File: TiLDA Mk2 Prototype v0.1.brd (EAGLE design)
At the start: 67.9 x 100 mm, 199 parts, among them IC1 ATSAM3X8EA-AU, IC10 MCP73831, IC2 MPU-6050, IC3 SRF-V1.2, IC5 S25FL216K0PMFI011, IC7 HMC5883LSMD (NP), IC8 MCP1825T-3302E/DC, IC9 TC1015-3V3, J1 ZX62-AB-5PA(11), J3 Arduino Headers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

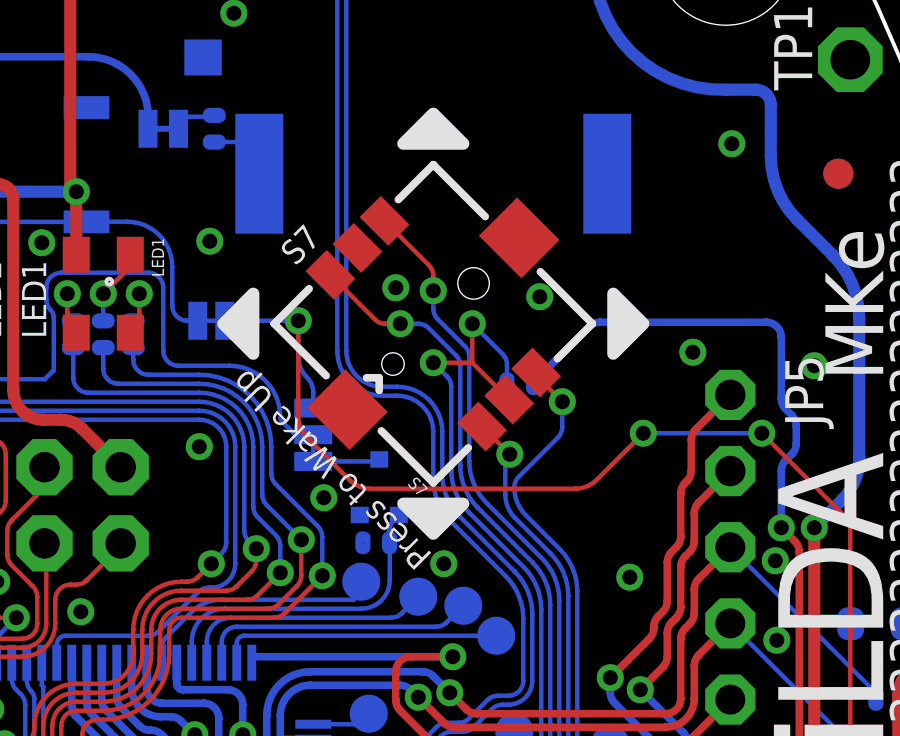
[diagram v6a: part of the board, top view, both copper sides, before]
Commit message: Parts: Joystick footprint Prototype: Joystick footprint
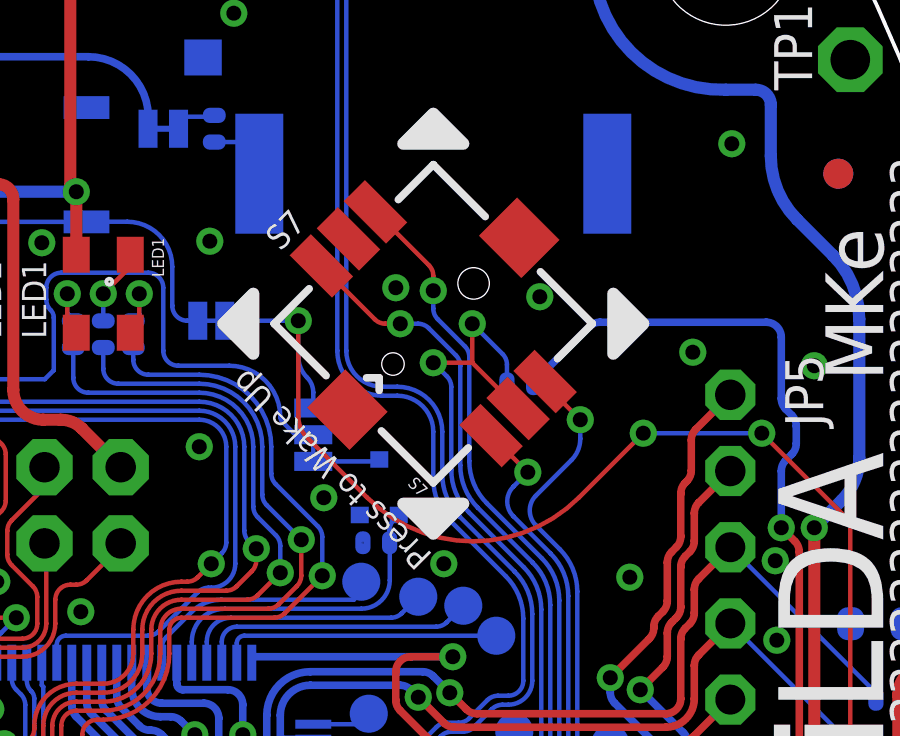
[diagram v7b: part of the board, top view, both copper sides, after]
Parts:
- S7: device TiLDA Mk2 Parts:JOYSTICK_MINI_ALPS -> TiLDA Mk2 Parts:JOYSTICK_MULTICOMP
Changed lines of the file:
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@@
 <text x="17.6" y="82.3" size="0.8128" layer="21" font="vector" ratio="15" rot="R90">S5</text>
 <text x="11.3" y="74.6" size="0.8128" layer="21" font="vector" ratio="15" rot="R90">S6</text>
-<text x="43.4" y="85.9" size="0.8128" layer="21" font="vector" ratio="15" rot="R45">S7</text>
+<text x="42.9" y="86.4" size="0.8128" layer="21" font="vector" ratio="15" rot="R45">S7</text>
 <text x="44.5" y="72.3" size="0.8128" layer="22" font="vector" ratio="15" rot="MR0">IC1</text>
 <text x="41.3" y="13.7" size="0.8128" layer="22" font="vector" ratio="15" rot="MR90">IC2</text>
@@
 <element name="S5" library="TiLDA Mk2 Parts" package="TACTILE_SWITCH_SMD" value="SKQGAKE010" x="20.5" y="83.9" rot="R90"/>
 <element name="S6" library="TiLDA Mk2 Parts" package="TACTILE_SWITCH_SMD" value="SKQGAKE010" x="14" y="77.9" rot="R90"/>
-<element name="S7" library="TiLDA Mk2 Parts" package="JOYSTICK_MINI_ALPS" value="SKRHAAE010" x="48" y="84" rot="R135"/>
+<element name="S7" library="TiLDA Mk2 Parts" package="JOYSTICK_MULTICOMP" value="SKRHAAE010" x="48" y="84" rot="R135"/>
 <element name="SJ5" library="TiLDA Mk2 Parts" package="SJ_3" value="RESET SELECT" x="37.4" y="38.8" rot="MR0"/>
 <element name="R21" library="TiLDA Mk2 Parts" package="R0402-ARDUINO-ROUND" value="0402/100K/1%" x="60.7" y="61.44" rot="MR0"/>
@@
 <wire x1="55" y1="80.35" x2="58.95" y2="80.35" width="0.15" layer="16"/>
 <wire x1="58.95" y1="80.35" x2="61.753553125" y2="77.546446875" width="0.15" layer="1"/>
-<wire x1="55" y1="80.35" x2="53.44289375" y2="78.79289375" width="0.15" layer="1"/>
-<wire x1="53.44289375" y1="78.79289375" x2="52.7357875" y2="78.5" width="0.15" layer="1" curve="-45"/>
-<wire x1="52.7357875" y1="78.5" x2="45.9142125" y2="78.5" width="0.15" layer="1"/>
-<wire x1="45.9142125" y1="78.5" x2="45.20710625" y2="78.79289375" width="0.15" layer="1" curve="-45"/>
-<wire x1="45.20710625" y1="78.79289375" x2="43.79289375" y2="80.20710625" width="0.15" layer="1"/>
+<wire x1="55" y1="80.35" x2="52.860534375" y2="78.210534375" width="0.15" layer="1"/>
+<wire x1="52.860534375" y1="78.210534375" x2="45.789465625" y2="78.210534375" width="0.15" layer="1" curve="-90"/>
+<wire x1="45.789465625" y1="78.210534375" x2="43.79289375" y2="80.20710625" width="0.15" layer="1"/>
 <wire x1="43.79289375" y1="80.20710625" x2="43.5" y2="80.9142125" width="0.15" layer="1" curve="-45"/>
 <wire x1="43.5" y1="80.9142125" x2="43.5" y2="84.1" width="0.15" layer="1"/>
@@
 <wire x1="48" y1="82.7" x2="48.453553125" y2="82.246446875" width="0.15" layer="16"/>
 <wire x1="48.453553125" y1="82.246446875" x2="48.6" y2="81.89289375" width="0.15" layer="16" curve="-45"/>
-<wire x1="50.52790625" y1="81.472090625" x2="49.3" y2="82.699996875" width="0.15" layer="1"/>
+<wire x1="50.828425" y1="81.171571875" x2="49.3" y2="82.699996875" width="0.15" layer="1"/>
 <wire x1="49.3" y1="82.699996875" x2="49.299996875" y2="82.7" width="0.15" layer="1"/>
 <wire x1="49.299996875" y1="82.7" x2="48" y2="82.7" width="0.15" layer="1"/>
@@
 <wire x1="47.846446875" y1="83.853553125" x2="48.753553125" y2="82.946446875" width="0.15" layer="16"/>
 <wire x1="48.753553125" y1="82.946446875" x2="48.9" y2="82.59289375" width="0.15" layer="16" curve="-45"/>
-<wire x1="44.57053125" y1="85.62634375" x2="46.050428125" y2="84.146446875" width="0.15" layer="1"/>
+<wire x1="44.270009375" y1="85.926865625" x2="46.050428125" y2="84.146446875" width="0.15" layer="1"/>
 <wire x1="46.050428125" y1="84.146446875" x2="46.40398125" y2="84" width="0.15" layer="1" curve="45"/>
 <wire x1="46.40398125" y1="84" x2="46.9" y2="84" width="0.15" layer="1"/>
@@
 <wire x1="52.5" y1="64.85" x2="52.5" y2="74.921571875" width="0.15" layer="16"/>
 <wire x1="52.5" y1="74.921571875" x2="51.9142125" y2="76.3357875" width="0.15" layer="16" curve="45.000063"/>
-<wire x1="51.9142125" y1="76.3357875" x2="50.72218125" y2="77.52781875" width="0.15" layer="16"/>
-<wire x1="50.72218125" y1="77.52781875" x2="50.4" y2="78.305634375" width="0.15" layer="16" curve="-44.999837"/>
-<wire x1="50.4" y1="78.305634375" x2="50.4" y2="79.5" width="0.15" layer="16"/>
-<via x="50.55" y="79.65" extent="1-16" drill="0.5"/>
-<wire x1="50.55" y1="79.65" x2="50.4" y2="79.5" width="0.15" layer="16"/>
-<wire x1="50.55" y1="79.65" x2="50.546875" y2="79.65" width="0.15" layer="1"/>
-<wire x1="50.546875" y1="79.65" x2="49.62634375" y2="80.57053125" width="0.15" layer="1"/>
+<wire x1="51.15" y1="79.05" x2="50.669975" y2="78.569975" width="0.15" layer="16"/>
+<wire x1="50.669975" y1="78.569975" x2="50.669975" y2="77.580025" width="0.15" layer="16" curve="90"/>
+<wire x1="50.669975" y1="77.580025" x2="51.9142125" y2="76.3357875" width="0.15" layer="16"/>
+<via x="51.15" y="79.05" extent="1-16" drill="0.5"/>
+<wire x1="51.15" y1="79.05" x2="51.146875" y2="79.05" width="0.15" layer="1"/>
+<wire x1="51.146875" y1="79.05" x2="49.926865625" y2="80.270009375" width="0.15" layer="1"/>
 </signal>
 <signal name="BUTTON_DOWN">
@@
 <wire x1="48.146446875" y1="84.153553125" x2="49.053553125" y2="83.246446875" width="0.15" layer="16"/>
 <wire x1="49.053553125" y1="83.246446875" x2="49.2" y2="82.89289375" width="0.15" layer="16" curve="-45"/>
-<wire x1="46.373653125" y1="87.429465625" x2="47.853553125" y2="85.949565625" width="0.15" layer="1"/>
+<wire x1="46.07313125" y1="87.7299875" x2="47.853553125" y2="85.949565625" width="0.15" layer="1"/>
 <wire x1="47.853553125" y1="85.949565625" x2="48" y2="85.5960125" width="0.15" layer="1" curve="-45"/>
 <wire x1="48" y1="85.5960125" x2="48" y2="85.1" width="0.15" layer="1"/>
@@
 <wire x1="52.8" y1="64.85" x2="52.8" y2="75.071571875" width="0.15" layer="16"/>
 <wire x1="52.8" y1="75.071571875" x2="52.2142125" y2="76.4857875" width="0.15" layer="16" curve="45.000063"/>
-<wire x1="50.7" y1="78.54289375" x2="51.083884375" y2="77.616115625" width="0.15" layer="16" curve="45"/>
-<wire x1="51.083884375" y1="77.616115625" x2="52.2142125" y2="76.4857875" width="0.15" layer="16"/>
-<wire x1="52.3" y1="81.4" x2="52.3" y2="80.55710625" width="0.15" layer="16"/>
-<wire x1="52.3" y1="80.55710625" x2="52.153553125" y2="80.203553125" width="0.15" layer="16" curve="-45"/>
-<wire x1="52.153553125" y1="80.203553125" x2="50.846446875" y2="78.896446875" width="0.15" layer="16"/>
-<wire x1="50.846446875" y1="78.896446875" x2="50.7" y2="78.54289375" width="0.15" layer="16" curve="45"/>
-<wire x1="51.429465625" y1="82.373653125" x2="51.429465625" y2="82.270534375" width="0.15" layer="1"/>
-<wire x1="51.429465625" y1="82.270534375" x2="52.3" y2="81.4" width="0.15" layer="1"/>
-<via x="52.3" y="81.4" extent="1-16" drill="0.5"/>
+<wire x1="52.9" y1="80.8" x2="52.9" y2="80.1642125" width="0.15" layer="16"/>
+<wire x1="52.9" y1="80.1642125" x2="52.60710625" y2="79.45710625" width="0.15" layer="16" curve="-45"/>
+<wire x1="52.60710625" y1="79.45710625" x2="51.419975" y2="78.269975" width="0.15" layer="16"/>
+<wire x1="51.419975" y1="78.269975" x2="51.419975" y2="77.280025" width="0.15" layer="16" curve="90"/>
+<wire x1="51.419975" y1="77.280025" x2="52.2142125" y2="76.4857875" width="0.15" layer="16"/>
+<via x="52.9" y="80.8" extent="1-16" drill="0.5"/>
+<wire x1="51.7299875" y1="82.07313125" x2="51.7299875" y2="81.9700125" width="0.15" layer="1"/>
+<wire x1="51.7299875" y1="81.9700125" x2="52.9" y2="80.8" width="0.15" layer="1"/>
 </signal>
 <signal name="BUTTON_UP1">

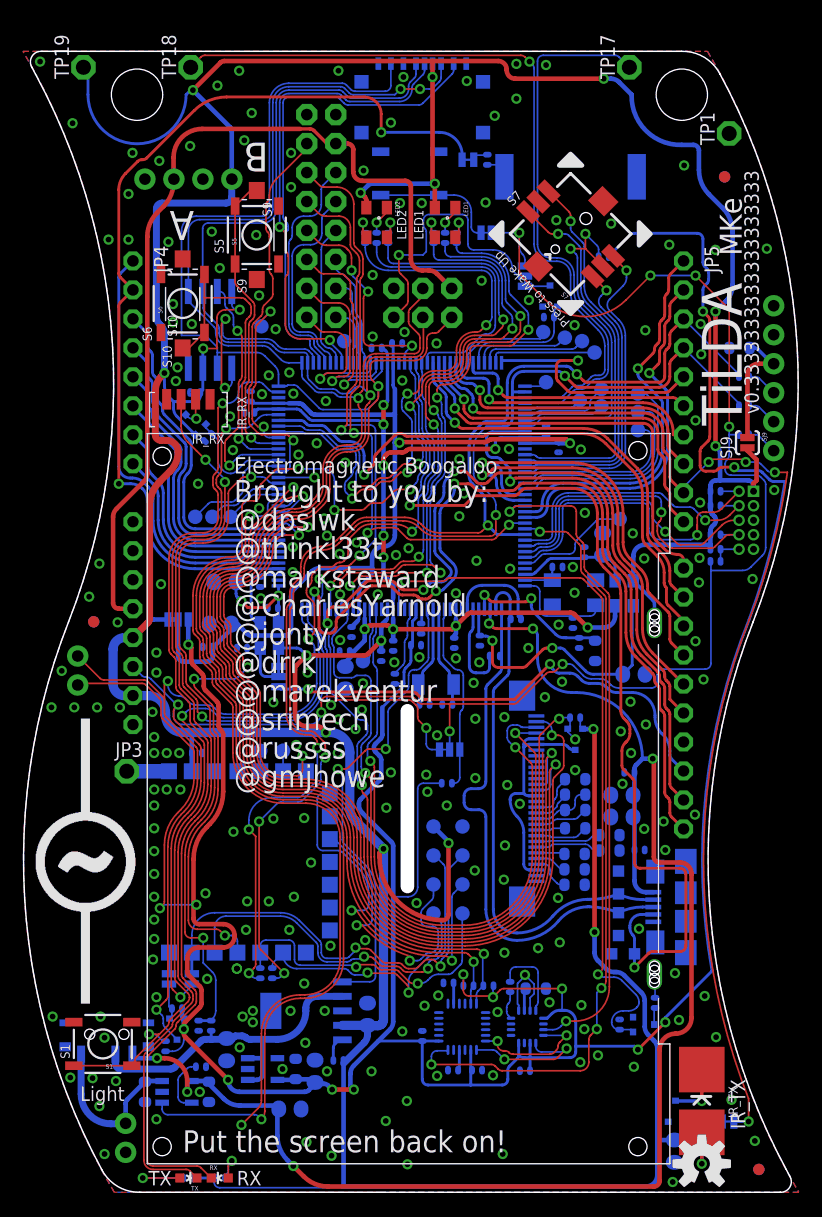
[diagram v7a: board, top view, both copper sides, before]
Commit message: Parts: Fix LCD footprint Prototype: Correct tracks fro LCD Footprint
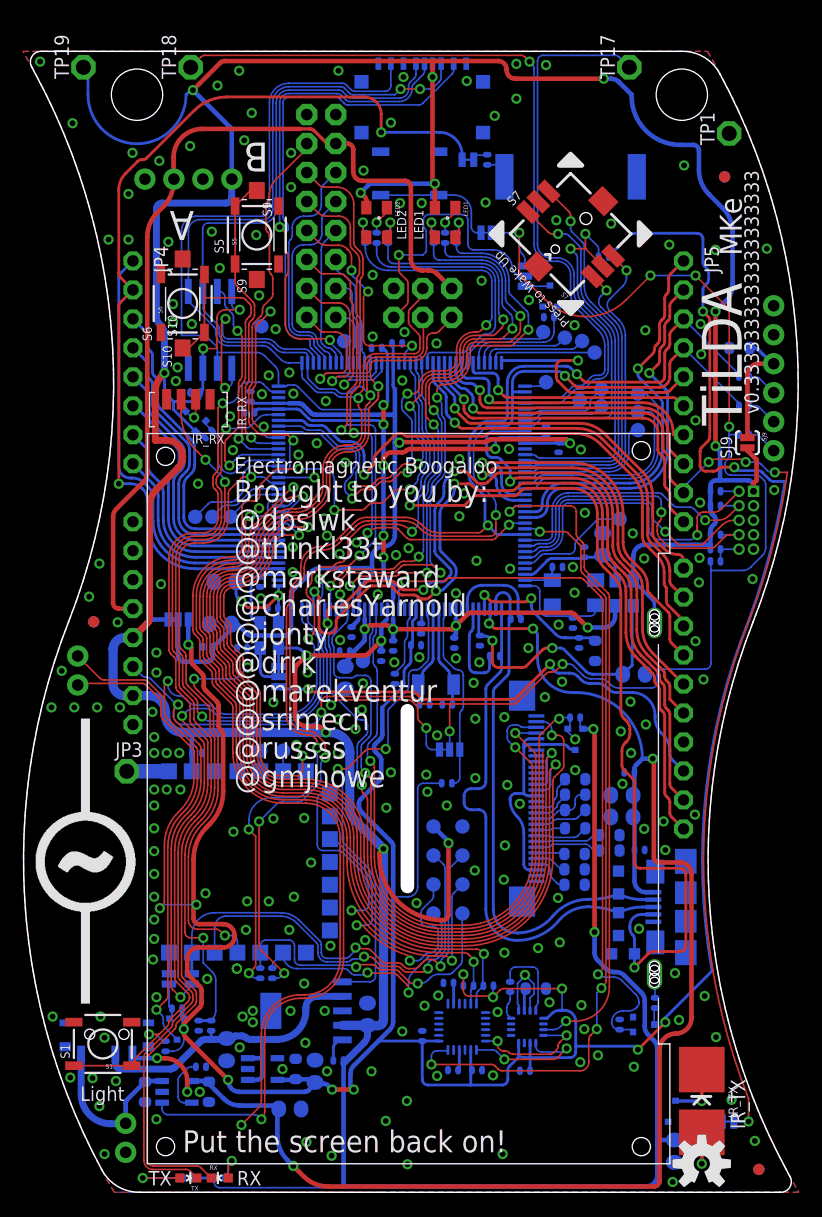
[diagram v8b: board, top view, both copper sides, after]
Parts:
- moved Q13 0.30 mm to (14.9, 67.8)
- moved R49 0.30 mm to (16.3, 66.5)
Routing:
- net PWM8: track 36.0 -> 33.1 mm
- net TXD0: track 14.6 -> 12.4 mm
- net AD2: track 22.2 -> 22.8 mm
- net 3V3: track 519.7 -> 520.2 mm
